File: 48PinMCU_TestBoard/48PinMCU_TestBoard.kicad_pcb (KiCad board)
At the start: 2 copper layers, 96 parts, among them IC1 TCAN3413DR, IC2 74LVC1G157GW,125, J1 SWD_Header_02x02, J2 USB_C_Receptacle_USB2.0_16P, J3 USB_C_Receptacle_USB2.0_16P, J5 Conn_01x20, J6 Conn_01x20, SW1 Reset, SW2 SW_SPDT, SW3 BOOT Switch, U1 STM32G431CBT6, U2 ESP32-C6-MINI-1, U3 MCP1826S, U4 TPS2117DRLR, Y1 Crystal

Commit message: preliminary layout blocks
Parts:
- removed JP1: TRM, Connector_PinHeader_2.54mm:PinHeader_1x02_P2.54mm_Vertical
- removed JP2, JP3, JP4, JP5, JP6, JP7: SolderJumper_2_Bridged, Jumper:SolderJumper-2_P1.3mm_Bridged_Pad1.0x1.5mm
- removed R26: 10k, Resistor_SMD:R_0603_1608Metric_Pad0.98x0.95mm_HandSolder
- removed REF**: SW_CJS-1200TA, UTSVT_Special:SW_CJS-1200TA
- added C18: 10uF, Capacitor_SMD:C_0805_2012Metric_Pad1.18x1.45mm_HandSolder, F.Cu at (49.3, 152.6)
- added D15: 1N5819HW-7-F, Diode_SMD:D_SOD-123, F.Cu at (48.9, 150.2)
- added D16: TPD2EUSB30DRTR, UTSVT_ICs:TPD2EUSB30DRTR, F.Cu at (45.3, 150.0)
- added D17: SBA130CH-AU_R1_000A1, Diode_SMD:D_SOD-323_HandSoldering, F.Cu at (119.0, 117.0)
- added D18: CDSOT23-T24CAN, UTSVT_Passives:CDSOT23-T24CAN, F.Cu at (178.2, 142.6)
- added J7: Conn_01x17, Connector_PinHeader_2.54mm:PinHeader_1x17_P2.54mm_Vertical, F.Cu at (93.6, 138.5)
- added J8: Conn_01x17, Connector_PinHeader_2.54mm:PinHeader_1x17_P2.54mm_Vertical, F.Cu at (98.2, 138.5)
- added JP10: SolderJumper_2_Open, Jumper:SolderJumper-2_P1.3mm_Open_Pad1.0x1.5mm, F.Cu at (102.7, 145.0)
- added JP11: SolderJumper_2_Open, Jumper:SolderJumper-2_P1.3mm_Open_Pad1.0x1.5mm, F.Cu at (102.7, 148.6)
- added JP12: SolderJumper_2_Open, Jumper:SolderJumper-2_P1.3mm_Open_Pad1.0x1.5mm, F.Cu at (102.7, 152.1)
- added JP13: SolderJumper_2_Open, Jumper:SolderJumper-2_P1.3mm_Open_Pad1.0x1.5mm, F.Cu at (102.7, 155.7)
- added JP14: SolderJumper_2_Open, Jumper:SolderJumper-2_P1.3mm_Open_Pad1.0x1.5mm, F.Cu at (102.7, 159.2)
- added JP15: TRM, Connector_PinHeader_2.54mm:PinHeader_1x02_P2.54mm_Vertical, F.Cu at (160.5, 175.5)
- added JP9: SolderJumper_2_Open, Jumper:SolderJumper-2_P1.3mm_Open_Pad1.0x1.5mm, F.Cu at (102.7, 141.5)
- added R29: 10k, Resistor_SMD:R_0603_1608Metric_Pad0.98x0.95mm_HandSolder, F.Cu at (106.2, 122.4)
- added R30: 60, Resistor_SMD:R_0603_1608Metric_Pad0.98x0.95mm_HandSolder, F.Cu at (153.5, 174.3)
- added R31: 60, Resistor_SMD:R_0603_1608Metric_Pad0.98x0.95mm_HandSolder, F.Cu at (153.3, 177.3)
- added SW4: RESET Button, UTSVT_ESP32:TL3365AF180QG, F.Cu at (67.4, 164.0)
- added TP1: GND_TP, TestPoint:TestPoint_THTPad_3.0x3.0mm_Drill1.5mm, F.Cu at (108.6, 137.4)
- added TP2: GND_TP, TestPoint:TestPoint_THTPad_3.0x3.0mm_Drill1.5mm, F.Cu at (108.6, 142.4)
- added TP3: GND_TP, TestPoint:TestPoint_THTPad_3.0x3.0mm_Drill1.5mm, F.Cu at (108.6, 147.5)
- added TP4: GND_TP, TestPoint:TestPoint_THTPad_3.0x3.0mm_Drill1.5mm, F.Cu at (108.6, 152.6)
- C1: value 26p -> 10uF; footprint Capacitor_SMD:C_0603_1608Metric_Pad1.08x0.95mm_HandSolder -> Capacitor_SMD:C_0805_2012Metric_Pad1.18x1.45mm_HandSolder
- C10, C12: value 0.1uF -> 1uF
- C11, C9: value 1uF -> 0.1uF
- C15: value 100nF -> 0.1uF
- C16: value 10uF -> 100nF; footprint Capacitor_SMD:C_0805_2012Metric_Pad1.18x1.45mm_HandSolder -> Capacitor_SMD:C_0603_1608Metric_Pad1.08x0.95mm_HandSolder
- C22, C4: value 10uF -> 0.1uF; footprint Capacitor_SMD:C_0805_2012Metric_Pad1.18x1.45mm_HandSolder -> Capacitor_SMD:C_0603_1608Metric_Pad1.08x0.95mm_HandSolder
- C23: value 0.1uF -> 10u; footprint Capacitor_SMD:C_0603_1608Metric_Pad1.08x0.95mm_HandSolder -> Capacitor_SMD:C_0805_2012Metric_Pad1.18x1.45mm_HandSolder
- C24: value 0.1uF -> 0.1u
- C26: value 10u -> 0.1uF; footprint Capacitor_SMD:C_0805_2012Metric_Pad1.18x1.45mm_HandSolder -> Capacitor_SMD:C_0603_1608Metric_Pad1.08x0.95mm_HandSolder
- C28: value 0.1u -> 0.1uF
- C3: value 0.1uF -> 26p
- C5: value 0.1uF -> 10uF; footprint Capacitor_SMD:C_0603_1608Metric_Pad1.08x0.95mm_HandSolder -> Capacitor_SMD:C_0805_2012Metric_Pad1.18x1.45mm_HandSolder
- D1: value D_TVS -> 1N5819HW-7-F; footprint Diode_SMD:D_SOD-323 -> Diode_SMD:D_SOD-123
- D10: value CDSOT23-T24CAN -> BOOT; footprint UTSVT_Passives:CDSOT23-T24CAN -> Diode_SMD:D_0603_1608Metric
- D11: value 1N5819HW-7-F -> +3.3V_ESP; footprint Diode_SMD:D_SOD-123 -> Diode_SMD:D_0603_1608Metric
- D12: value MCU_LED1 -> VBUS_IN
- D13: value MCU_LED2 -> ESP_LED1
- D14: value TPD2EUSB30DRTR -> ESP_LED2; footprint UTSVT_ICs:TPD2EUSB30DRTR -> Diode_SMD:D_0603_1608Metric
- D2: value LED -> TPD2EUSB30DRTR; footprint LED_SMD:LED_0201_0603Metric -> UTSVT_ICs:TPD2EUSB30DRTR
- D3: value +3.3V_ESP -> MCU_LED1
- D4: value VBUS_IN -> MCU_LED2
- D5: value ESP_LED1 -> +3.3V_LED
- D6: value ESP_LED2 -> +5V_LED
- D7: value 1N5819HW-7-F -> +5V_MCU_LED; footprint Diode_SMD:D_SOD-123 -> Diode_SMD:D_0603_1608Metric
- D8: value TPD2EUSB30DRTR -> +5V_ESP_LED; footprint UTSVT_ICs:TPD2EUSB30DRTR -> Diode_SMD:D_0603_1608Metric
- D9: value SBA130CH-AU_R1_000A1 -> D_TVS; footprint Diode_SMD:D_SOD-323_HandSoldering -> Diode_SMD:D_SOD-323
- IC1: value TCAN3413DR -> 74LVC1G157GW,125; footprint UTSVT_Passives:TCAN3413DR -> UTSVT_ICs:SOP65P210X110-6N
- IC2: value 74LVC1G157GW,125 -> TCAN3413DR; footprint UTSVT_ICs:74LVC1G157GW,125 -> UTSVT_Passives:TCAN3413DR
- J1: value SWD_Header_02x02 -> USB_C_Receptacle_USB2.0_16P; footprint UTSVT_Connectors:Molex_Nano-Fit_105309-xx04_1x04_P2.50mm_Vertical -> UTSVT_Connectors:USB_C_Receptacle_GCT_USB4105-xx-A_16P_TopMnt_Horizontal
- J2: value USB_C_Receptacle_USB2.0_16P -> CAN_Nanofit; footprint UTSVT_Connectors:USB_C_Receptacle_GCT_USB4105-xx-A_16P_TopMnt_Horizontal -> UTSVT_Connectors:Molex_Nano-Fit_105309-xx02_1x02_P2.50mm_Vertical
- J3: value USB_C_Receptacle_USB2.0_16P -> Conn_01x03; footprint UTSVT_Connectors:USB_C_Receptacle_GCT_USB4105-xx-A_16P_TopMnt_Horizontal -> Connector_PinHeader_2.54mm:PinHeader_1x03_P2.54mm_Vertical
- J5: value Conn_01x20 -> SWD_Header_02x02; footprint Connector_PinHeader_2.54mm:PinHeader_1x20_P2.54mm_Vertical -> UTSVT_Connectors:Molex_Nano-Fit_105309-xx04_1x04_P2.50mm_Vertical
- J6: value Conn_01x20 -> USB_C_Receptacle_USB2.0_16P; footprint Connector_PinHeader_2.54mm:PinHeader_1x20_P2.54mm_Vertical -> UTSVT_Connectors:USB_C_Receptacle_GCT_USB4105-xx-A_16P_TopMnt_Horizontal
- JP8: value SolderJumper_2_Bridged -> SolderJumper_2_Open; footprint Jumper:SolderJumper-2_P1.3mm_Bridged_Pad1.0x1.5mm -> Jumper:SolderJumper-2_P1.3mm_Open_Pad1.0x1.5mm
- R10, R11: value 5.1k -> 2.2k
- R12, R20: value 10k -> 2.2k
- R15, R16: value 5.1k -> 22
- R18, R19: value 60 -> 1k
- R2: value 22 -> 10k
- R21: value 10k -> 1k
- R22: value 16k -> 1k
- R23: value 4.7k -> 5.1k
- R24: value 1k -> 5.1k
- R25: value 1k -> 10k
- R3: value 22 -> 5.1k
- R4: value 10k -> 5.1k
- R5: value 1k -> 16k
- R6: value 1k -> 4.7k
- R7: value 2.2k -> 1k
- moved U2 382.0 mm to (62.7, 143.4), turned to 0 degrees
- moved SW3 358.0 mm to (77.4, 163.9)
- moved R7 354.9 mm to (107.2, 168.8), turned to 0 degrees
- moved D7 350.0 mm to (116.7, 171.8), turned to 0 degrees
- moved D8 349.3 mm to (116.7, 174.4), turned to 0 degrees
- moved R11 349.3 mm to (111.6, 168.8), turned to 0 degrees
- moved R10 347.0 mm to (111.6, 166.3), turned to 0 degrees
- moved D4 344.7 mm to (116.7, 164.0), turned to 0 degrees
- moved C16 325.9 mm to (138.8, 153.8), turned to -90 degrees
- moved C19 323.9 mm to (66.5, 159.4)
- moved R21 323.2 mm to (73.3, 151.7)
- moved R12 292.4 mm to (111.6, 171.3)
- moved R8 292.4 mm to (107.2, 171.3)
- moved J2 286.9 mm to (173.6, 141.6), turned to 0 degrees
- moved D3 285.9 mm to (116.7, 161.4)
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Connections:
- C1 pad 1: Net-(U1-PF0-OSC_IN) -> +5V_MCU
- C10 pad 1: +3.3V -> /MCU/VDDA
- C10 pad 2: GND -> /MCU/GNDA
- C12 pad 1: +3.3V -> /MCU/VDDA
- C12 pad 2: GND -> /MCU/GNDA
- C16 pad 1: +5V_ESP -> /MCU/VDDA
- C16 pad 2: GND -> /MCU/GNDA
- C2 pad 1: GND -> Net-(U1-PF0-OSC_IN)
- C2 pad 2: Net-(U1-PF1-OSC_OUT) -> GND
- C20 pad 2: Net-(D9-K) -> Net-(D17-K)
- C23 pad 1: +5V_MCU -> +3.3V
- C24 pad 1: +5V_ESP -> +3.3V
- C25 pad 1: /Power Mux/PR1 -> +5V_ESP
- C26 pad 1: +3.3V -> /Power Mux/PR1
- C28 pad 1: +3.3V -> +5V
- C3 pad 1: +3.3V -> GND
- C3 pad 2: GND -> Net-(U1-PF1-OSC_OUT)
- C30 pad 1: +5V -> +3.3V
- C4 pad 1: +3.3V -> /MCU/VDDA
- C4 pad 2: GND -> /MCU/GNDA
- C5 pad 1: /MCU_RESET_M -> +3.3V
- C6 pad 1: +3.3V -> /MCU_RESET_M
- C8 pad 1: +3.3V -> /MCU/VDDA
- C8 pad 2: GND -> /MCU/GNDA
- D1 pad 1: GND -> +5V_MCU
- D1 pad 2: Net-(D1-A2) -> /VBUS
- D10 pad 1: /CAN_H -> Net-(D10-K)
- D10 pad 2: /CAN_L -> Net-(D10-A)
- D11 pad 1: +5V_MCU -> GND
- D11 pad 2: /VBUSB -> Net-(D11-A)
- D14 pad 1: /USB_D- -> GND
- D14 pad 2: /USB_D+ -> Net-(D14-A)
- D2 pad 1: Net-(D2-K) -> /USB_D-
- D2 pad 2: Net-(D1-A2) -> /USB_D+
- D7 pad 1: +5V_ESP -> GND
- D7 pad 2: /ESP32/VBUSB -> Net-(D7-A)
- D8 pad 1: /ESP32/USB_D- -> GND
- D8 pad 2: /ESP32/USB_D+ -> Net-(D8-A)
- D9 pad 1: Net-(D9-K) -> GND
- D9 pad 2: +5V -> Net-(D10-A)
- FB1 pad 1: GND -> /MCU/GNDA
- FB2 pad 2: +3.3V -> /MCU/VDDA
- IC1 pad 1: /CAN_TX -> /CAN_RX
- IC1 pad 3: +3.3V -> /MCU_BOOT0_M
- IC1 pad 4: /CAN_RX -> /MCU/CAN_RX/BOOT0
- IC1 pad 6: /CAN_L -> /MCU/CAN_EN
- IC2 pad 1: /CAN_RX -> /CAN_TX
- IC2 pad 3: /MCU_BOOT0_M -> +3.3V
- IC2 pad 4: /MCU/CAN_RX/BOOT0 -> /CAN_RX
- IC2 pad 6: /MCU/CAN_EN -> /CAN_L
- J5 pad 2: +5V_ESP -> GND
- J5 pad 3: /CAN_TX -> Net-(J5-Pin_3)
- J5 pad 4: /CAN_H -> Net-(J5-Pin_4)
- JP8 pad 1: /MCU_RESET_M -> /ESP_RESET_M
- JP8 pad 2: /MCU_RESET_E -> /ESP_RESET_E
- R1 pad 1: /MCU_RESET_M -> +3.3V
- R1 pad 2: +3.3V -> /I2C_SCL
- R10 pad 1: Net-(J2-CC1) -> +5V
- R10 pad 2: GND -> Net-(D6-A)
- R11 pad 1: Net-(J2-CC2) -> +5V_MCU
- R11 pad 2: GND -> Net-(D7-A)
- R12 pad 1: /ESP32/BOOT -> +5V_ESP
- R12 pad 2: Net-(SW3-B) -> Net-(D8-A)
- R13 pad 1: +3.3V -> GND
- R13 pad 2: /ESP_RESET_E -> /MCU/CAN_EN
- R14 pad 1: Net-(U2-GPIO8) -> /MCU_RESET_M
- R15 pad 1: Net-(J3-CC1) -> /MCU/SWCLK
- R15 pad 2: GND -> Net-(J5-Pin_3)
- R16 pad 1: Net-(J3-CC2) -> /MCU/SWDIO
- R16 pad 2: GND -> Net-(J5-Pin_4)
- R17 pad 1: +5V_MCU -> /MCU_BOOT0_M
- R17 pad 2: Net-(U4-ST) -> Net-(D10-A)
- R18 pad 1: /CAN_H -> Net-(D10-K)
- R18 pad 2: Net-(C29-Pad2) -> GND
- R19 pad 1: Net-(C29-Pad2) -> +3.3V
- R19 pad 2: Net-(JP1-A) -> Net-(D11-A)
- R2 pad 1: /MCU/SWCLK -> +3.3V
- R2 pad 2: Net-(J1-Pin_3) -> /I2C_SDA
- R20 pad 1: GND -> /ESP32/VBUS
- R20 pad 2: /MCU/CAN_EN -> Net-(D12-A)
- R21 pad 1: +3.3V -> /ESP32/LED1
- R21 pad 2: /ESP_RESET_E -> Net-(D13-A)
- R22 pad 1: +5V_MCU -> /ESP32/LED2
- R22 pad 2: /Power Mux/PR1 -> Net-(D14-A)
- R23 pad 1: /Power Mux/PR1 -> Net-(J6-CC1)
- R24 pad 1: /MCU_LED_1 -> Net-(J6-CC2)
- R24 pad 2: Net-(D12-A) -> GND
- R25 pad 1: /MCU_LED_2 -> /ESP32/BOOT
- R25 pad 2: Net-(D13-A) -> Net-(SW3-B)
- R27 pad 2: /I2C_SCL -> /ESP_RESET_E
- R28 pad 1: +3.3V -> Net-(U2-GPIO8)
- R28 pad 2: /SPI_NSS -> +3.3V
- R3 pad 1: /MCU/SWDIO -> Net-(J1-CC1)
- R3 pad 2: Net-(J1-Pin_4) -> GND
- R4 pad 1: /MCU_BOOT0_M -> Net-(J1-CC2)
- R4 pad 2: Net-(D1-A2) -> GND
- R5 pad 1: Net-(D2-K) -> +5V_MCU
- R5 pad 2: GND -> /Power Mux/PR1
- R6 pad 1: +3.3V -> /Power Mux/PR1
- R6 pad 2: Net-(D3-A) -> GND
- R7 pad 1: /ESP32/VBUSB -> /MCU_LED_1
- R7 pad 2: Net-(D4-A) -> Net-(D3-A)
- R8 pad 1: /ESP32/LED1 -> /MCU_LED_2
- R8 pad 2: Net-(D5-A) -> Net-(D4-A)
- R9 pad 1: /ESP32/LED2 -> +3.3V
- R9 pad 2: Net-(D6-A) -> Net-(D5-A)
- SW2 pad 2: Net-(D1-A2) -> Net-(D10-A)
- U1 pad 19: GND -> /MCU/GNDA
- U1 pad 2: /PC13 -> /MCU/PC13
- U1 pad 20: +3.3V -> /MCU/VDDA
- U1 pad 21: +3.3V -> /MCU/VDDA
- U1 pad 3: /PC14 -> /MCU/PC14
- U1 pad 4: /PC15 -> /MCU/PC15
- U3 pad 1: Net-(D9-K) -> Net-(D17-K)
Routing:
- net +3.3V: track 0.00 -> 115.4 mm, vias 0 -> 2
- net /ESP_RESET_E: track 0.00 -> 22.5 mm, vias 0 -> 2
- net /ESP32/USB_D+: track 10.1 -> 29.3 mm
- net /ESP32/USB_D-: track 9.66 -> 27.5 mm
- net /ESP32/VBUS: track 0.00 -> 15.7 mm, vias 0 -> 2
- net /ESP32/BOOT: track 0.00 -> 14.9 mm, vias 0 -> 2
- net /MCU/VDDA: track 0.00 -> 14.7 mm
- net /MCU/GNDA: track 0.00 -> 13.7 mm, vias 0 -> 2
- net Net-(J2-CC1): track 12.2 -> 0.00 mm
- net Net-(D10-A): track 0.00 -> 10.9 mm
- net /CAN_L: track 0.00 -> 10.8 mm, vias 0 -> 2
- net /VBUS: track 0.00 -> 9.49 mm
- net Net-(J2-CC2): track 9.39 -> 0.00 mm
- net /ESP32/VBUSB: track 9.02 -> 0.00 mm, vias 2 -> 0
- net Net-(J1-CC1): track 0.00 -> 8.23 mm, vias 0 -> 2
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- removed copper zone on F.Cu, net /ESP32/VBUSB
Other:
- board text added: "CAN Mux"
- board text added: "CAN Transceiver"
- board text added: "ESP RESET & BOOT"
- board text added: "ESP USB Input"
- board text added: "ESP32"
- board text added: "LDO"
- board text added: "MCU RESET & BOOT"
- board text added: "MCU USB Input"
- board text added: "Power Mux"
- board text added: "STM32G431CBT6"

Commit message: Layout
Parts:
- J5: value SWD_Header_02x02 -> SWD
- JP10: value SolderJumper_2_Open -> UART_RX
- JP11: value SolderJumper_2_Open -> GPIO1
- JP12: value SolderJumper_2_Open -> GPIO2
- JP13: value SolderJumper_2_Open -> MCU_BOOT
- JP14: value SolderJumper_2_Open -> MCU_RESET
- JP8: value SolderJumper_2_Open -> ESP_RESET
- JP9: value SolderJumper_2_Open -> UART_TX
- TP1, TP2, TP3, TP4: value GND_TP -> GND; footprint TestPoint:TestPoint_THTPad_3.0x3.0mm_Drill1.5mm -> TestPoint:TestPoint_Keystone_5005-5009_Compact
- moved D16 133.9 mm to (152.5, 69.9)
- moved R19 133.9 mm to (180.6, 63.5)
- moved R21 133.9 mm to (180.5, 71.5)
- moved R22 133.9 mm to (180.5, 67.5)
- moved C18 133.9 mm to (156.5, 72.5)
- moved C19 133.9 mm to (173.7, 79.3)
- moved D11 133.9 mm to (185.9, 63.5)
- moved D12 133.9 mm to (156.0, 74.4)
- moved D13 133.9 mm to (185.9, 71.5)
- moved D14 133.9 mm to (185.9, 67.5)
- moved D15 133.9 mm to (156.1, 70.1)
- moved R20 133.9 mm to (149.6, 73.8)
- moved R23 133.9 mm to (149.6, 71.9)
- moved R24 133.9 mm to (149.5, 69.7)
- moved R25 133.9 mm to (181.5, 77.7)
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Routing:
- net +3.3V: track 115.4 -> 307.1 mm, vias 2 -> 4
- net /MCU_RESET_M: track 4.60 -> 167.8 mm, vias 0 -> 15
- net /MCU_BOOT0_M: track 0.00 -> 151.3 mm, vias 0 -> 10
- net /CAN_TX: track 0.00 -> 141.3 mm, vias 0 -> 8
- net /ESP_UART_TX_M: track 0.00 -> 123.4 mm, vias 0 -> 14
- net /ESP_RESET_M: track 0.00 -> 121.6 mm, vias 0 -> 6
- net /ESP_BREAKOUT1_M: track 0.00 -> 103.4 mm, vias 0 -> 6
- net /CAN_RX: track 0.00 -> 101.9 mm, vias 0 -> 4
- net /ESP_UART_RX_M: track 0.00 -> 100.2 mm, vias 0 -> 10
- net /ESP_BREAKOUT2_M: track 0.00 -> 99.8 mm, vias 0 -> 10
- net /ESP_BREAKOUT2_E: track 0.00 -> 94.9 mm, vias 0 -> 3
- net /CAN_H: track 2.94 -> 88.9 mm, vias 0 -> 4
- net /ESP_UART_RX_E: track 0.00 -> 85.5 mm, vias 0 -> 3
- net /MCU_LED_2: track 0.00 -> 84.3 mm, vias 0 -> 7
- net /ESP_UART_TX_E: track 0.00 -> 81.8 mm, vias 0 -> 4
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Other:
- board outline added: 112.1 x 57.3 mm
- board text added: "+3.3V"
- board text added: "+5V"
- board text added: "ADC_IN1"
- board text added: "ADC_IN2"
- board text added: "CAN_H"
- board text added: "CAN_L"
- board text added: "CAN_RX"
- board text added: "CAN_TX"
- board text added: "CLK"
- board text added: "ESP"
- board text added: "ESP_RESET"
- board text added: "GND"
- board text added: "GPIO1"
- board text added: "GPIO2"
- board text added: "I2C_SCL"
- board text added: "I2C_SDA"
- board text added: "IO"
- board text added: "MCU"
- board text added: "MCU_BOOT0"
- board text added: "MCU_LED1"
- board text added: "MCU_LED2"
- board text added: "MCU_RESET"
- board text added: "MUX"
- board text added: "PA10"
- board text added: "PB11"
- board text added: "PB12"
- board text added: "PB13"
- board text added: "PB14"
- board text added: "PB15"
- board text added: "PB4"
- board text added: "PB5"
- board text added: "PB6"
- board text added: "PB7"
- board text added: "RevX 48PinMCU/ESP Testboard"
- board text added: "SPI_MISO"
- board text added: "SPI_MOSI"
- board text added: "SPI_NSS"
- board text added: "SPI_SCK"
- board text added: "UART_RX"
- board text added: "UART_TX"

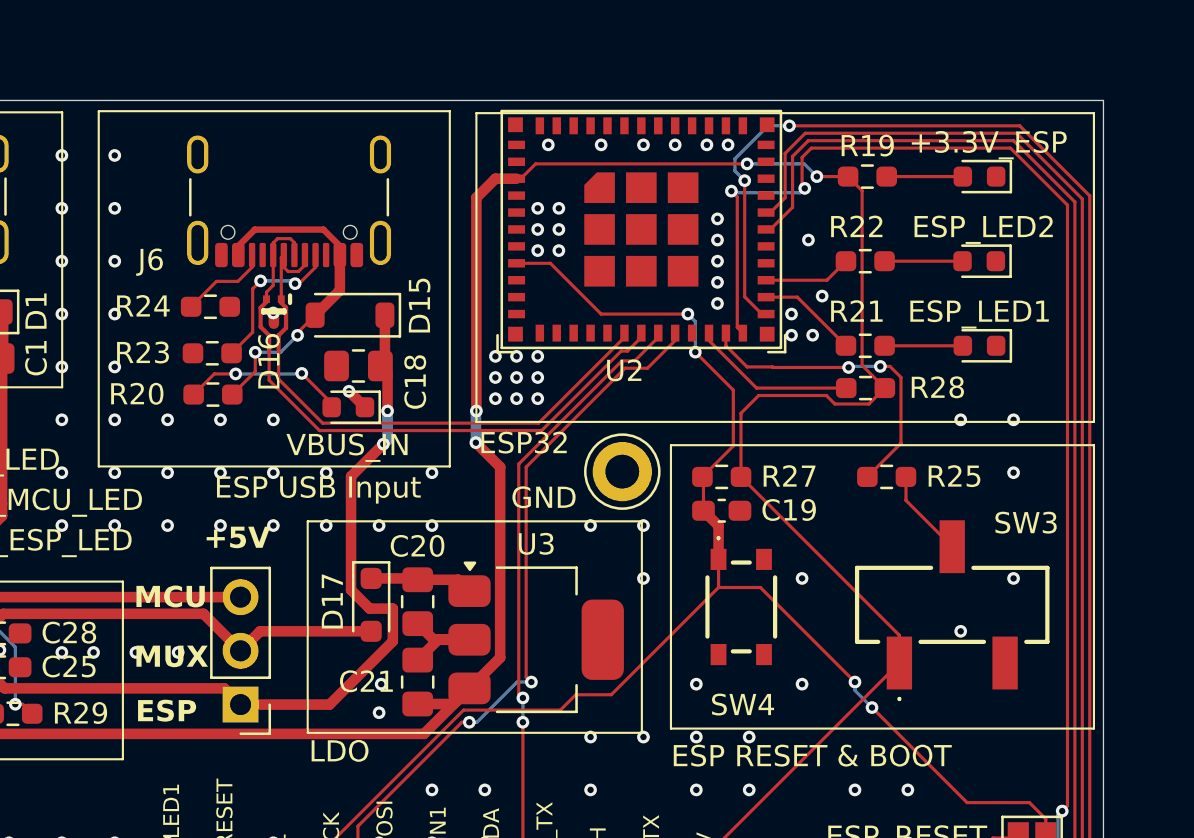
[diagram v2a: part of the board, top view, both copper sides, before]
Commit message: added bypass caps in series with ESP DC input
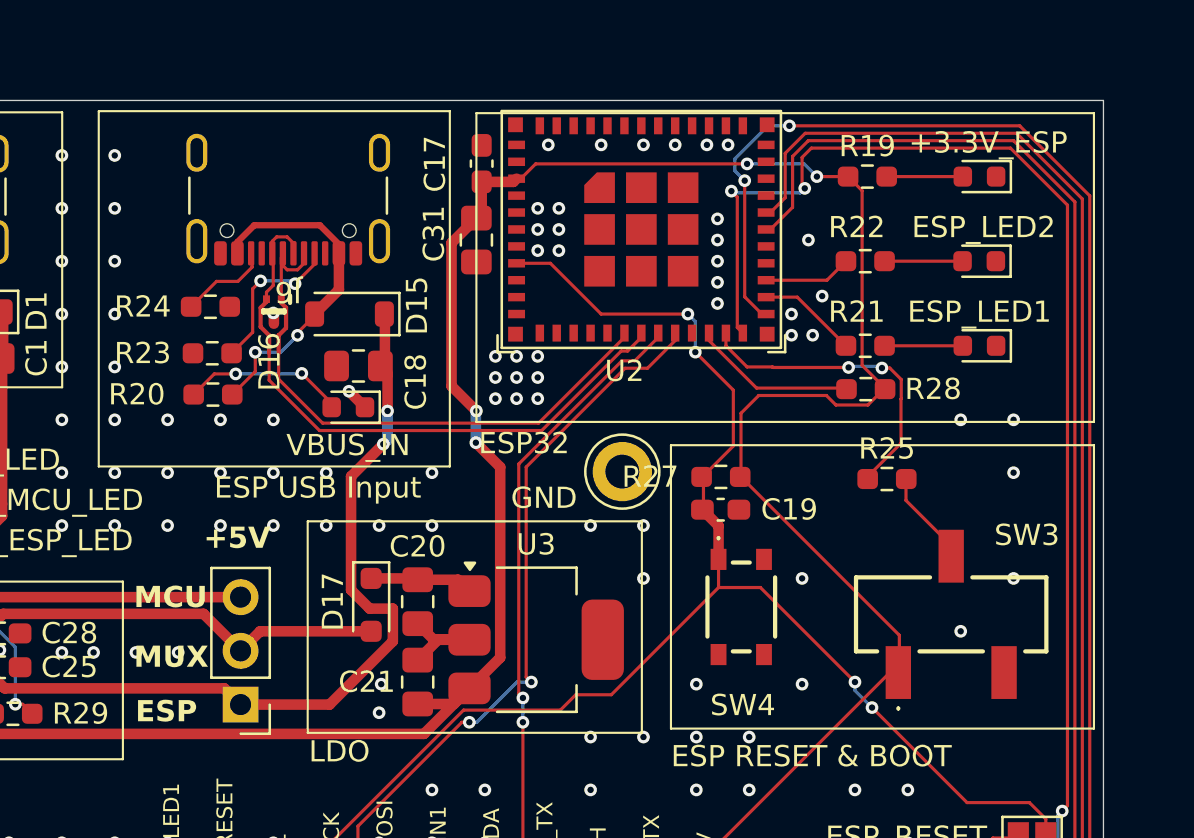
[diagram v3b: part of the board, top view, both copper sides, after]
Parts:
- added C17: 0.1uF, Capacitor_SMD:C_0603_1608Metric_Pad1.08x0.95mm_HandSolder, F.Cu at (162.3, 62.9)
- added C31: 10uF, Capacitor_SMD:C_0805_2012Metric_Pad1.18x1.45mm_HandSolder, F.Cu at (162.1, 66.5)
- moved SW3 0.45 mm to (184.6, 84.2)
- moved R25 0.10 mm to (181.5, 77.8)
- moved J6 0.09 mm to (153.2, 63.5)
- moved C19 0.07 mm to (173.7, 79.2)
- moved D15 0.06 mm to (156.1, 70.0)
- moved R28 0.05 mm to (180.5, 73.5)
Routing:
- net +3.3V: track 307.1 -> 308.6 mm
- net /ESP32/USB_D+: track 29.1 -> 30.2 mm
- net /ESP32/VBUS: track 14.9 -> 15.9 mm

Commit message: layout tweaks
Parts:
- removed J5: SWD, UTSVT_Connectors:Molex_Nano-Fit_105309-xx04_1x04_P2.50mm_Vertical
- added J4: SWD, Connector_PinHeader_2.54mm:PinHeader_1x04_P2.54mm_Vertical, F.Cu at (111.4, 64.0)
- JP10, JP11, JP12, JP13, JP14, JP8, JP9: footprint Jumper:SolderJumper-2_P1.3mm_Open_Pad1.0x1.5mm -> Jumper:SolderJumper-2_P1.3mm_Open_TrianglePad1.0x1.5mm
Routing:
- net +3.3V: track 308.6 -> 310.4 mm
- net Net-(J4-Pin_3): track 11.1 -> 12.0 mm
- net /I2C_SDA: track 58.1 -> 59.0 mm
- net /PA10: track 47.1 -> 47.8 mm
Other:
- board size 112.1 x 57.3 mm -> 114 x 57 mm

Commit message: made more changes!!
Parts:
- added J5: SWD, UTSVT_Connectors:CONN04_878320406_MOL, F.Cu at (119.6, 66.0)
- moved TP1 24.8 mm to (81.8, 62.8)
- moved J4 9.37 mm to (103.0, 68.2)
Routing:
- net +3.3V: track 310.4 -> 332.3 mm
- net Net-(J4-Pin_4): track 12.1 -> 21.6 mm, vias 0 -> 1
- net Net-(J4-Pin_3): track 12.0 -> 19.6 mm, vias 0 -> 1
- net /ESP32/USB_D+: track 30.2 -> 29.1 mm
- net /CAN_H: track 88.9 -> 89.9 mm
- net /ESP_RESET_E: track 74.7 -> 75.2 mm, vias 4 -> 6
- net GND: track 28.4 -> 28.3 mm, vias 257 -> 250
